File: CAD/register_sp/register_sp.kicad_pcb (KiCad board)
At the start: 2 copper layers, 90 x 45 mm, 58 parts, among them J1 Conn_01x18_Pin, J2 Conn_01x18_Pin, U1 74HC377, U2 74HC245, U3 74HC283, U4 74HC283, U5 74HC157, U6 74HC157, U7 74HC02, U8 74HC08

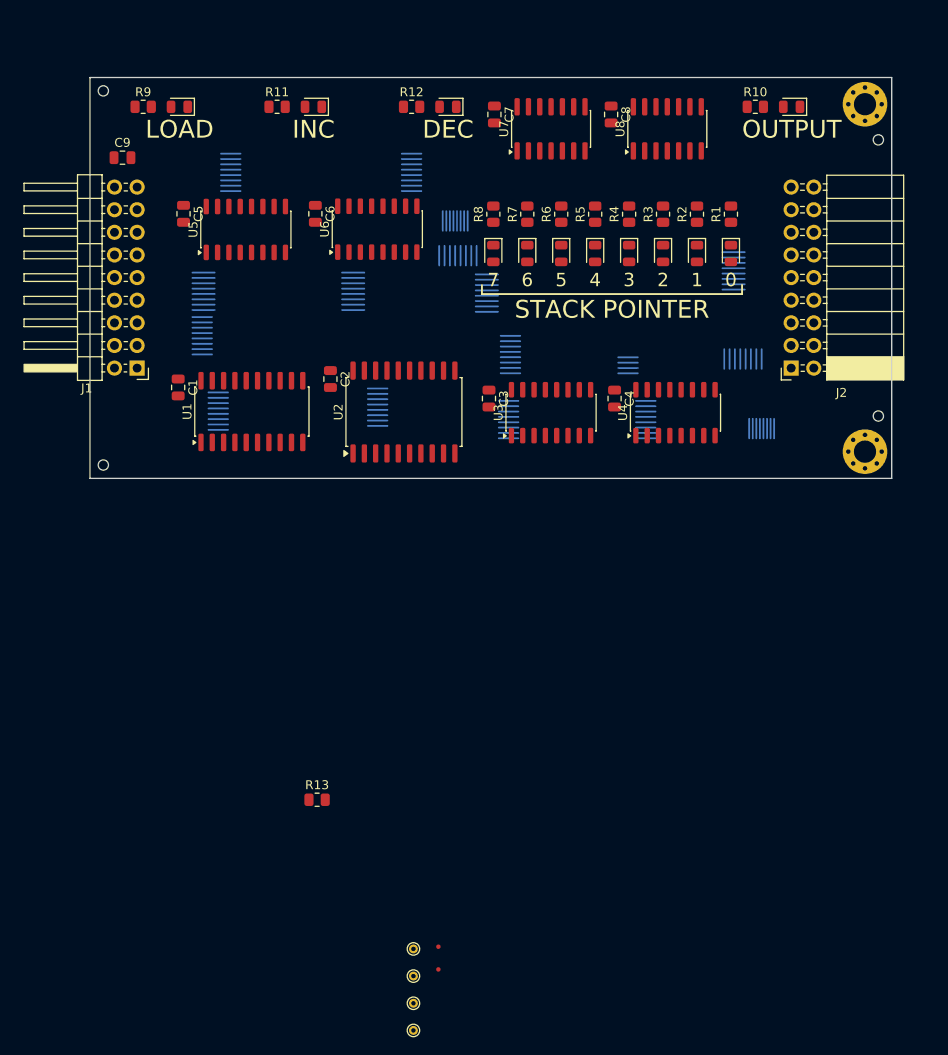
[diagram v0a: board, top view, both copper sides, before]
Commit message: add SP PCB
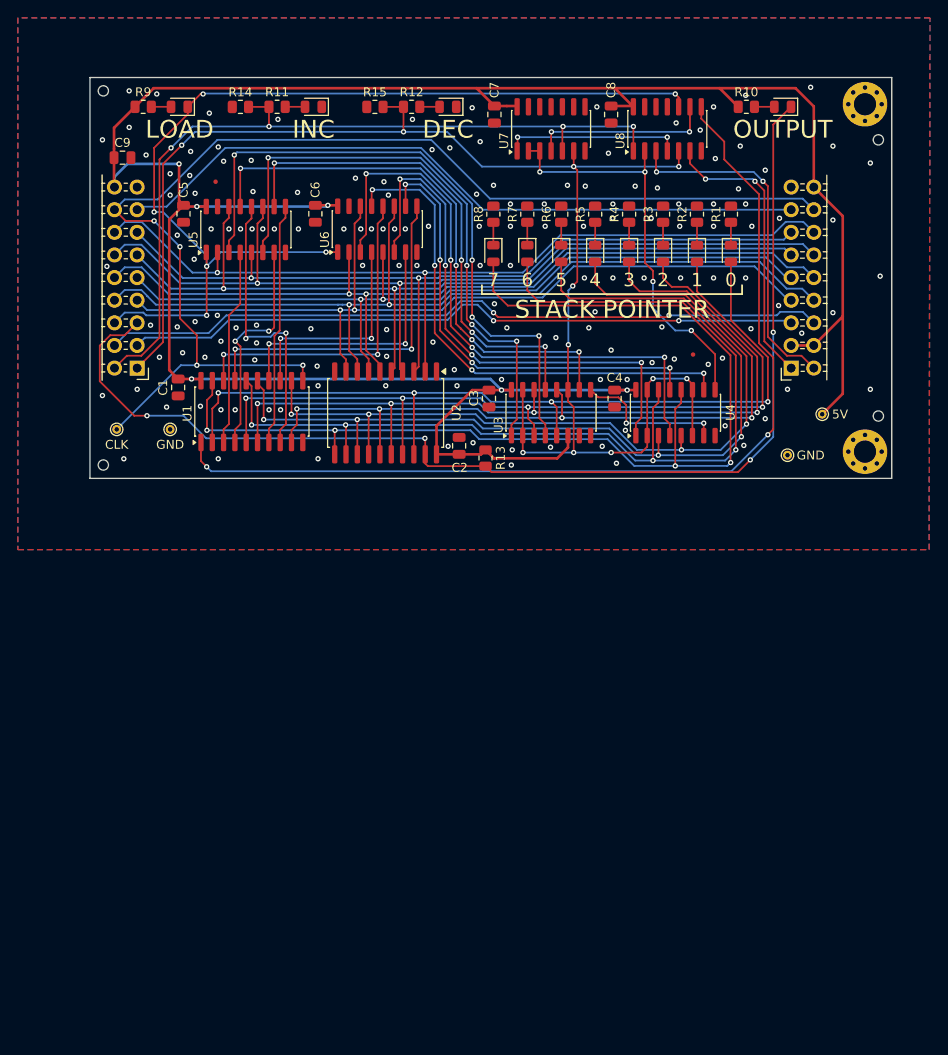
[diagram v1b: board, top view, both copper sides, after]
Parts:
- added R14: 10k, Resistor_SMD:R_0805_2012Metric, F.Cu at (76.9, 34.3)
- added R15: 10k, Resistor_SMD:R_0805_2012Metric, F.Cu at (92.0, 34.3)
- moved G*** 148.9 mm to (90.4, 36.9)
- moved FID1 89.4 mm to (74.1, 42.7)
- moved TP1 75.6 mm to (142.2, 68.8)
- moved FID2 74.7 mm to (127.7, 62.1)
- moved TP4 72.8 mm to (69.0, 70.5)
- moved TP3 72.5 mm to (63.0, 70.5)
- moved TP2 72.0 mm to (138.3, 73.4)
- moved Ref** 59.3 mm to (123.8, 49.3)
- moved R13 42.8 mm to (104.4, 73.7), turned to 90 degrees
- moved C2 16.3 mm to (101.4, 72.3), turned to 90 degrees
- moved U2 2.06 mm to (93.2, 68.7), turned to -90 degrees
- moved D10 1.01 mm to (137.8, 34.3)
- moved R10 1.01 mm to (133.7, 34.3)
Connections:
- J2 pad 3: unconnected-(J2-Pin_3-Pad3) -> +5V
- J2 pad 4: unconnected-(J2-Pin_4-Pad4) -> +5V
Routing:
- net +5V: track 0.00 -> 285.1 mm, vias 0 -> 6
- net dec: track 0.00 -> 166.4 mm, vias 0 -> 11
- net clk: track 0.00 -> 133.8 mm, vias 0 -> 4
- net ~{reg1_out}: track 0.00 -> 130.2 mm, vias 0 -> 4
- net ~{reg1_in}: track 0.00 -> 112.9 mm, vias 0 -> 6
- net /q7: track 13.2 -> 122.9 mm, vias 0 -> 4
- net /~{reg_load}: track 0.00 -> 108.3 mm, vias 0 -> 2
- net /q6: track 13.2 -> 113.5 mm, vias 0 -> 4
- net /dbus6: track 10.0 -> 102.6 mm, vias 0 -> 2
- net /dbus2: track 10.0 -> 102.0 mm, vias 0 -> 2
- net inc: track 0.00 -> 91.2 mm, vias 0 -> 4
- net /q5: track 13.2 -> 102.4 mm, vias 0 -> 4
- net /dbus0: track 10.0 -> 97.6 mm, vias 0 -> 2
- net /dbus4: track 10.0 -> 97.3 mm, vias 0 -> 2
- net /dbus7: track 10.0 -> 96.6 mm, vias 0 -> 2
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- added copper zone on B.Cu, net GND
- added copper zone on F.Cu, net GND
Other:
- board text added: "5V"
- board text added: "CLK"
- board text added: "GND"

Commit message: SP layout improvements
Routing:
- net /mux3: track 32.4 -> 35.5 mm
- net /add2: track 56.4 -> 54.5 mm
- net dec_out: track 32.2 -> 33.9 mm
- net inc_out: track 39.1 -> 40.7 mm
- net /add3: track 63.0 -> 61.9 mm
- net /carry_out: track 46.6 -> 47.6 mm
- net /dbus7: track 96.6 -> 95.6 mm
- net /add6: track 51.5 -> 52.4 mm
- net /add4: track 68.2 -> 67.2 mm
- net /add5: track 60.8 -> 59.8 mm
- net dec: track 166.4 -> 167.2 mm
- net /dbus4: track 97.3 -> 96.5 mm
- net /q0: track 96.3 -> 95.5 mm
- net ~{reg1_out}: track 130.2 -> 131.0 mm
- net /mux1: track 25.4 -> 24.7 mm
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
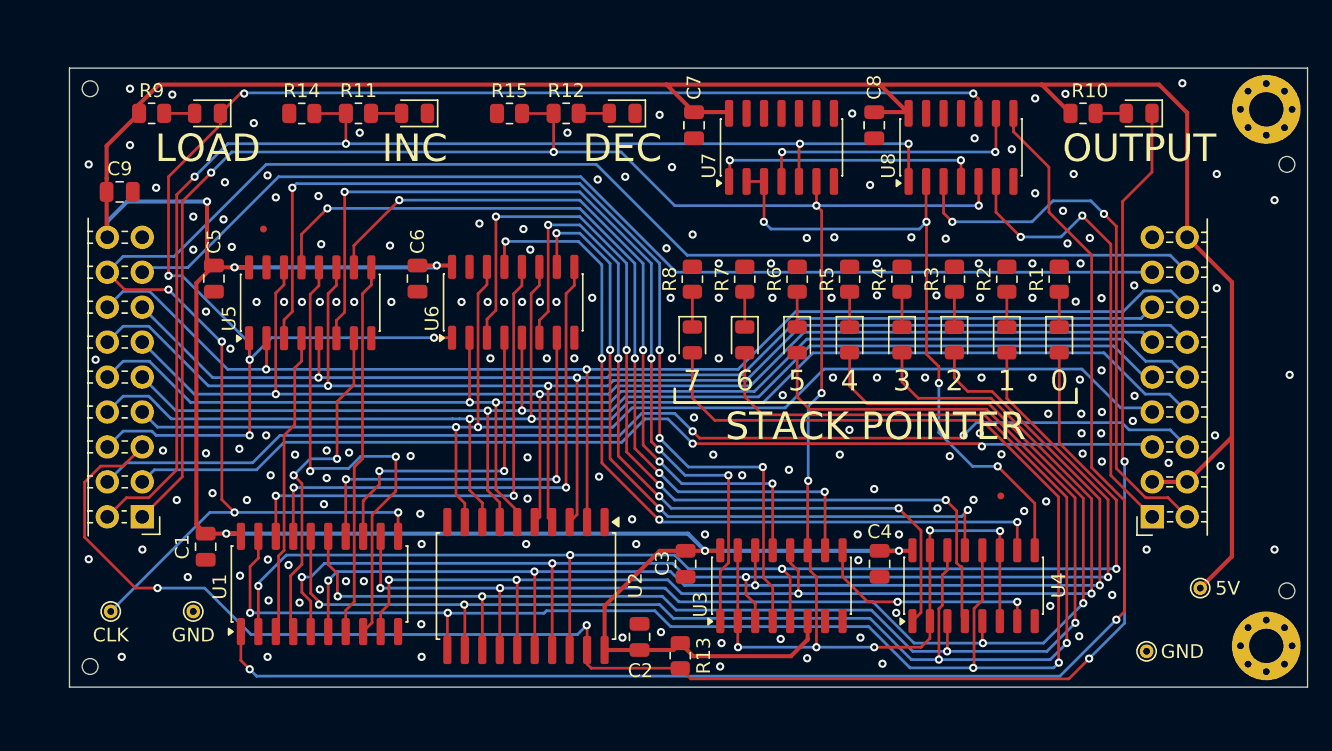
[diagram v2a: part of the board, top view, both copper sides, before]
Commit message: update SP - change board order
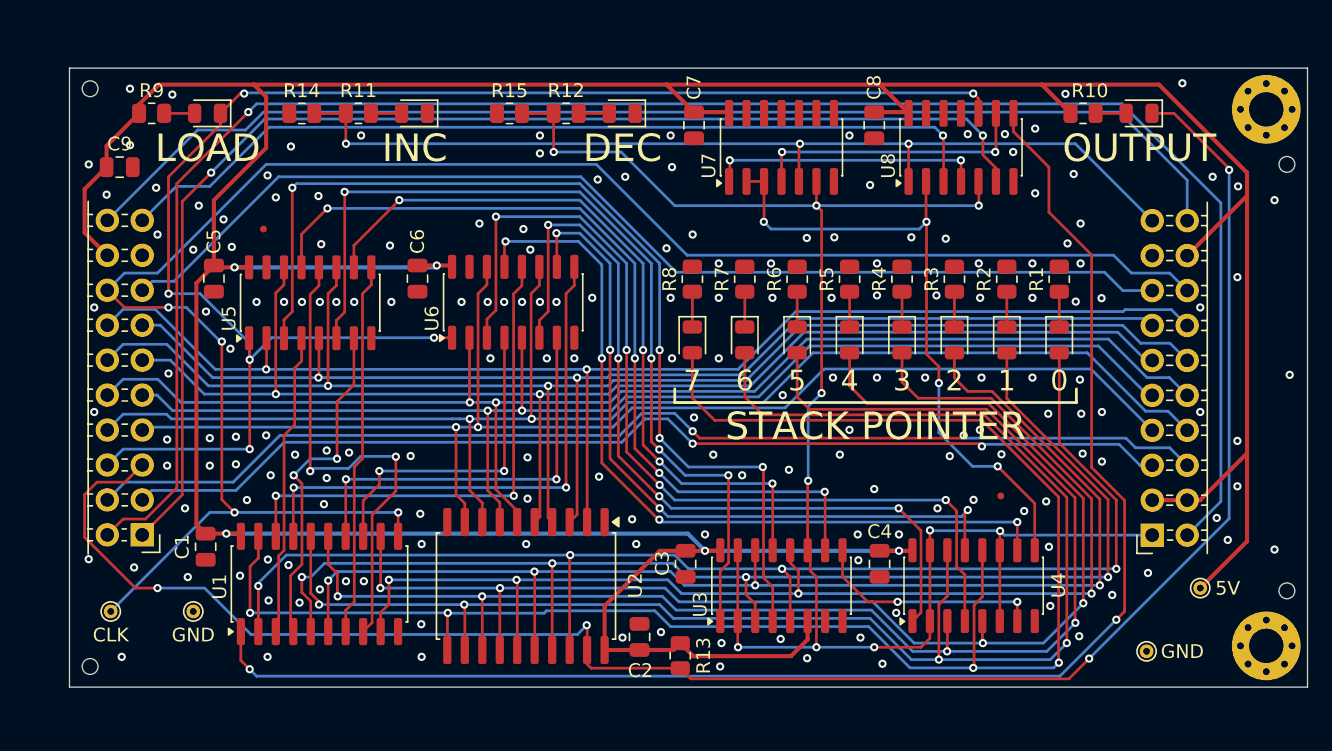
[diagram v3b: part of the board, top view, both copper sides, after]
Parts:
- J1: value Conn_01x18_Pin -> Conn_01x20_Pin; footprint Connector_PinHeader_2.54mm:PinHeader_2x09_P2.54mm_Horizontal -> Connector_PinHeader_2.54mm:PinHeader_2x10_P2.54mm_Horizontal
- J2: value Conn_01x18_Pin -> Conn_01x20_Pin; footprint Connector_PinSocket_2.54mm:PinSocket_2x09_P2.54mm_Horizontal -> Connector_PinSocket_2.54mm:PinSocket_2x10_P2.54mm_Horizontal
- moved C9 1.80 mm to (63.6, 38.2)
- moved J2 1.33 mm to (138.7, 65.0)
- moved J1 1.31 mm to (65.3, 64.9)
- moved G*** 0.80 mm to (89.6, 36.9)
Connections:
- J1 pad 1: dec -> dec_out
- J1 pad 2: inc -> dec_lsb
- J2 pad 1: dec_out -> dec_in
- J2 pad 2: inc_out -> dec_lsb
- R11 pad 1: inc -> inc_in
- R12 pad 1: dec -> dec_in
- R14 pad 2: inc -> inc_in
- R15 pad 2: dec -> dec_in
- U3 pad 11: dec -> dec_in
- U3 pad 15: dec -> dec_in
- U3 pad 2: dec -> dec_in
- U4 pad 11: dec -> dec_in
- U4 pad 15: dec -> dec_in
- U4 pad 2: dec -> dec_in
- U4 pad 6: dec -> dec_in
- U7 pad 5: inc -> inc_in
- U7 pad 6: dec -> dec_in
- U8 pad 1: inc -> inc_in
- U8 pad 5: dec -> dec_in
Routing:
- net dec: track 167.2 -> 0.00 mm, vias 11 -> 0
- net dec_lsb: track 0.00 -> 135.0 mm, vias 0 -> 1
- net dec_in: track 0.00 -> 125.8 mm, vias 0 -> 10
- net inc: track 91.2 -> 0.00 mm, vias 4 -> 0
- net inc_lsb: track 0.00 -> 86.8 mm
- net inc_in: track 0.00 -> 70.9 mm, vias 0 -> 3
- net dec_out: track 33.9 -> 90.4 mm
- net inc_out: track 40.7 -> 64.6 mm, vias 2 -> 1
- net +5V: track 284.4 -> 296.9 mm, vias 6 -> 5
- net ~{reg1_out}: track 131.0 -> 135.4 mm
- net ~{reg1_in}: track 112.8 -> 114.4 mm
- net ~{rst}: track 78.7 -> 80.3 mm
- net ~{reg2_out}: track 76.0 -> 77.4 mm
- net /dbus0: track 97.6 -> 96.4 mm
- net /dbus1: track 91.3 -> 90.6 mm
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
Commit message: SP layout improvements
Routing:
- net +5V: track 296.9 -> 300.5 mm
- net /q7: track 123.0 -> 121.1 mm
- net ~{reg1_out}: track 135.4 -> 136.8 mm
- net ~{reg1_in}: track 114.4 -> 115.4 mm
- net /dbus7: track 96.2 -> 95.3 mm
- net ~{reg2_in}: track 82.8 -> 83.6 mm
- net /dbus1: track 90.6 -> 89.9 mm
- net GND: vias 180 -> 193

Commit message: update SP label
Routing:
- net /add2: track 54.5 -> 55.3 mm
- net GND: vias 193 -> 192
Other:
- board text added: "8-BIT REGISTER /w INC & DEC"
- board text removed: "STACK POINTER"

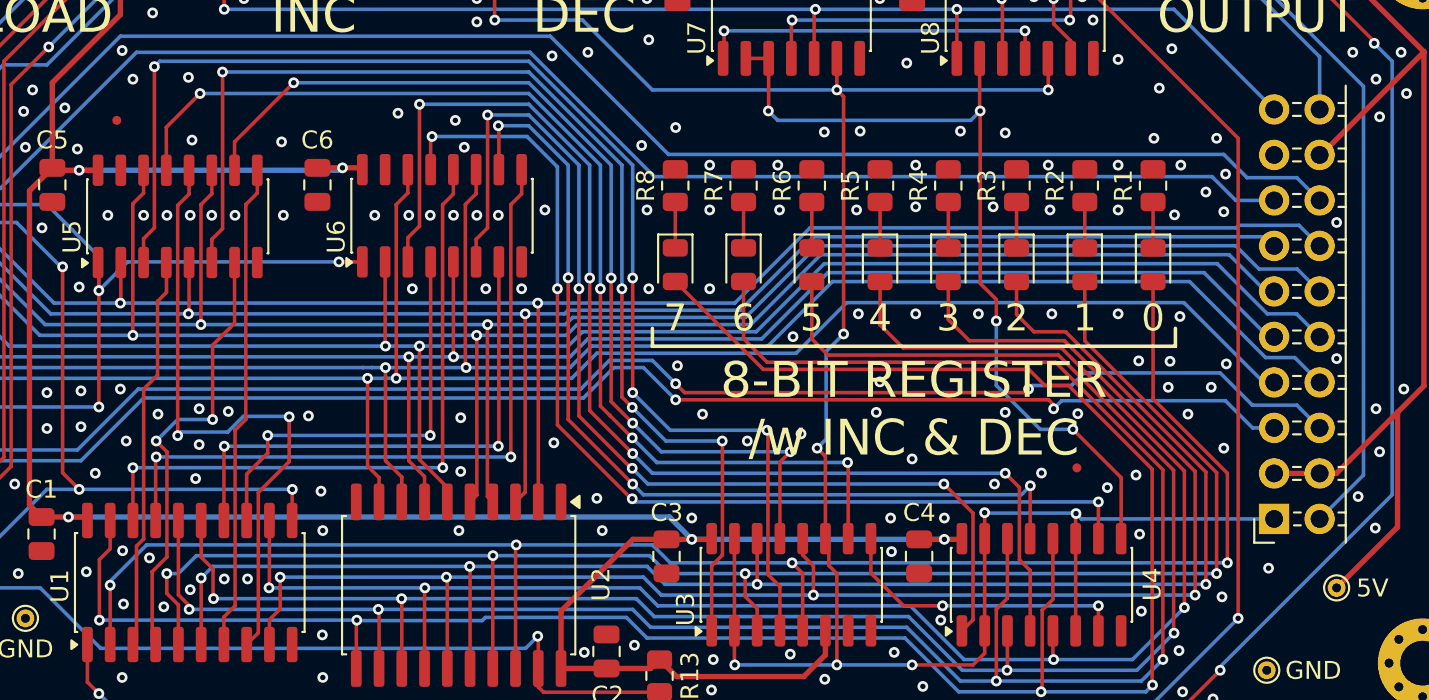
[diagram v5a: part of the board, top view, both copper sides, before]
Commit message: SP label improvements
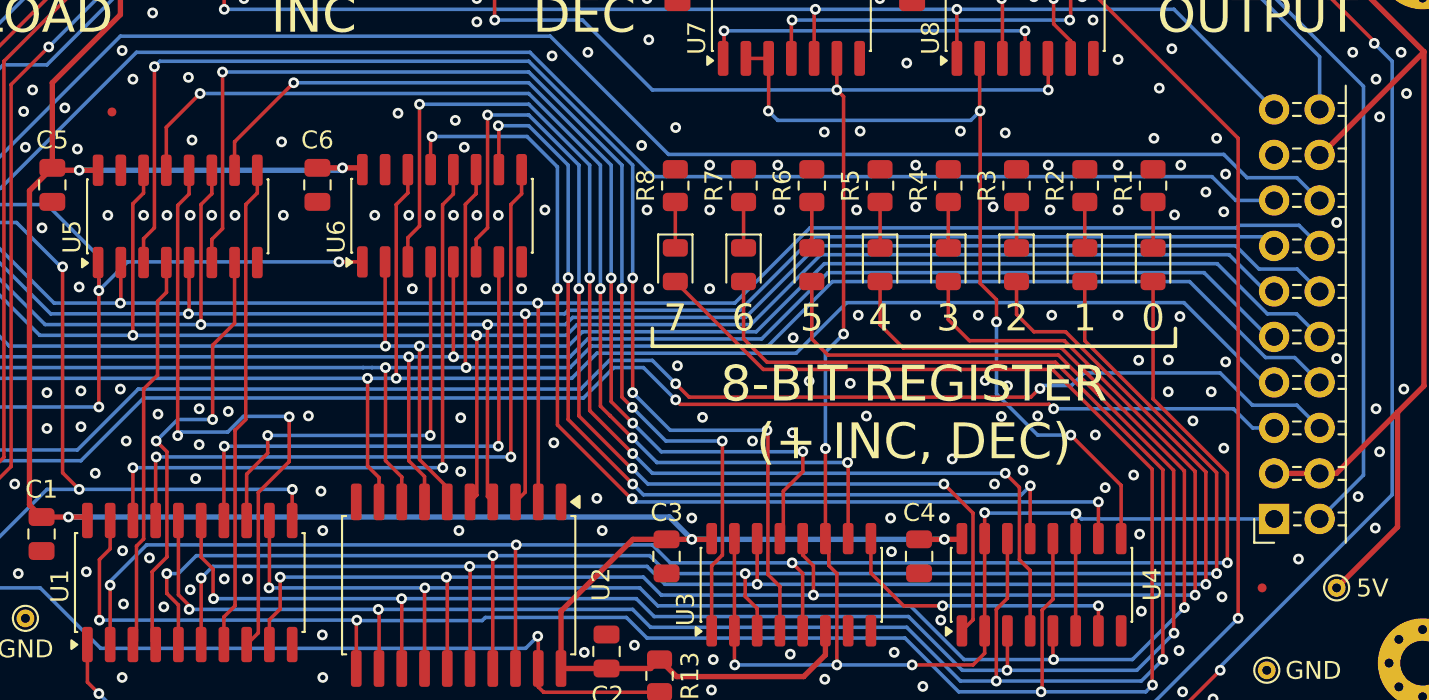
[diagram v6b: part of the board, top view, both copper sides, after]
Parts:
- moved FID2 12.3 mm to (138.0, 68.8)
- moved FID1 0.54 mm to (73.8, 42.2)
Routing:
- net /add2: track 55.3 -> 56.1 mm
- net GND: vias 192 -> 196
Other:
- board text added: "8-BIT REGISTER (+ INC, DEC)"
- board text removed: "8-BIT REGISTER /w INC & DEC"

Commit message: update KiCAD version 10.0
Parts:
- removed G***: LOGO, 8-bit_computer:qr-code-github
